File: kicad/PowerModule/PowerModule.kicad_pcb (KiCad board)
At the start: 4 copper layers, 85.6 x 54 mm, 58 parts, among them J1 DC+, J2 Power_out, J3 DC-, J4 105313-1206, Q3 EPC2304, Q4 EPC2304, Q5 EPC2304, Q6 EPC2304, U1 1EDN7550B, U2 1EDN7550B, U3 1EDN7550B, U4 1EDN7550B

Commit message: Power module: LS drivers next to the LS FETs, reference labels and owner block on silkscreen
- U2/U4 moved from the driver column to the top side between the phases, outputs facing the LS
  gate vias: driver -> gate path 4.8 mm (was 11-14 mm); HS 5.9-6.8 mm
- every reference designator on the silkscreen (0.8 mm, collision-checked placement)
- bottom silkscreen: owner name block, 2.3 mm text
- shield planes: 0.25 mm antipads and L2-L3 ties; centre-tap vias placed clear of the driver cells
- DRC with schematic parity: 0 violations, 0 unconnected, 0 parity issues

Co-Authored-By: Claude Opus 5.5 <noreply@anthropic.com>
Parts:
- moved D2 23.5 mm to (139.7, 128.3)
- moved R10 17.7 mm to (138.7, 126.1), turned to 180 degrees
- moved R6 17.3 mm to (132.1, 125.6)
- moved R5 17.1 mm to (132.1, 127.2)
- moved U2 16.0 mm to (135.4, 125.3), turned to 90 degrees
- moved C8 14.2 mm to (138.7, 124.4)
- moved D4 14.0 mm to (135.4, 139.4)
- moved R14 11.5 mm to (134.6, 121.6), turned to -90 degrees
- moved R13 10.6 mm to (136.2, 121.6), turned to -90 degrees
- moved R12 9.99 mm to (135.0, 137.3), turned to 180 degrees
- moved R3 9.20 mm to (132.1, 129.6)
- moved R4 8.83 mm to (132.1, 131.2)
- moved U4 8.25 mm to (135.4, 131.2), turned to -90 degrees
- moved C14 7.15 mm to (128.5, 132.2)
- moved R20 6.90 mm to (136.2, 134.8), turned to 90 degrees
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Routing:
- net +5V_iso: track 68.7 -> 92.6 mm
- net Net-(AT1-B1): track 5.71 -> 24.6 mm
- net GNDPWR: track 89.8 -> 76.6 mm, vias 396 -> 395
- net Net-(AT2-B1): track 8.62 -> 17.9 mm
- net /Gate_Drive/P1L: track 11.9 -> 2.77 mm
- net Net-(U2-IN-): track 8.57 -> 1.87 mm
- net /Gate_Drive/P2L: track 8.89 -> 2.77 mm
- net Net-(D4-K): track 8.33 -> 2.86 mm
- net Net-(U4-IN-): track 9.49 -> 4.12 mm
- net Net-(D2-K): track 7.92 -> 2.71 mm
- net Net-(U4-VDD): track 3.43 -> 6.07 mm
- net Net-(U2-IN+): track 1.91 -> 4.11 mm
- net Net-(AT2-B2): track 17.9 -> 16.6 mm, vias 2 -> 0
- net Net-(AT2-A2): track 5.50 -> 4.61 mm
- net +5V: track 49.0 -> 48.4 mm, vias 1 -> 2
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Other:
- board text added: "Tanishq Shendokar MS Electrical Engineering NC State University tsshendo@ncsu.edu +1 (336) 405-3942"

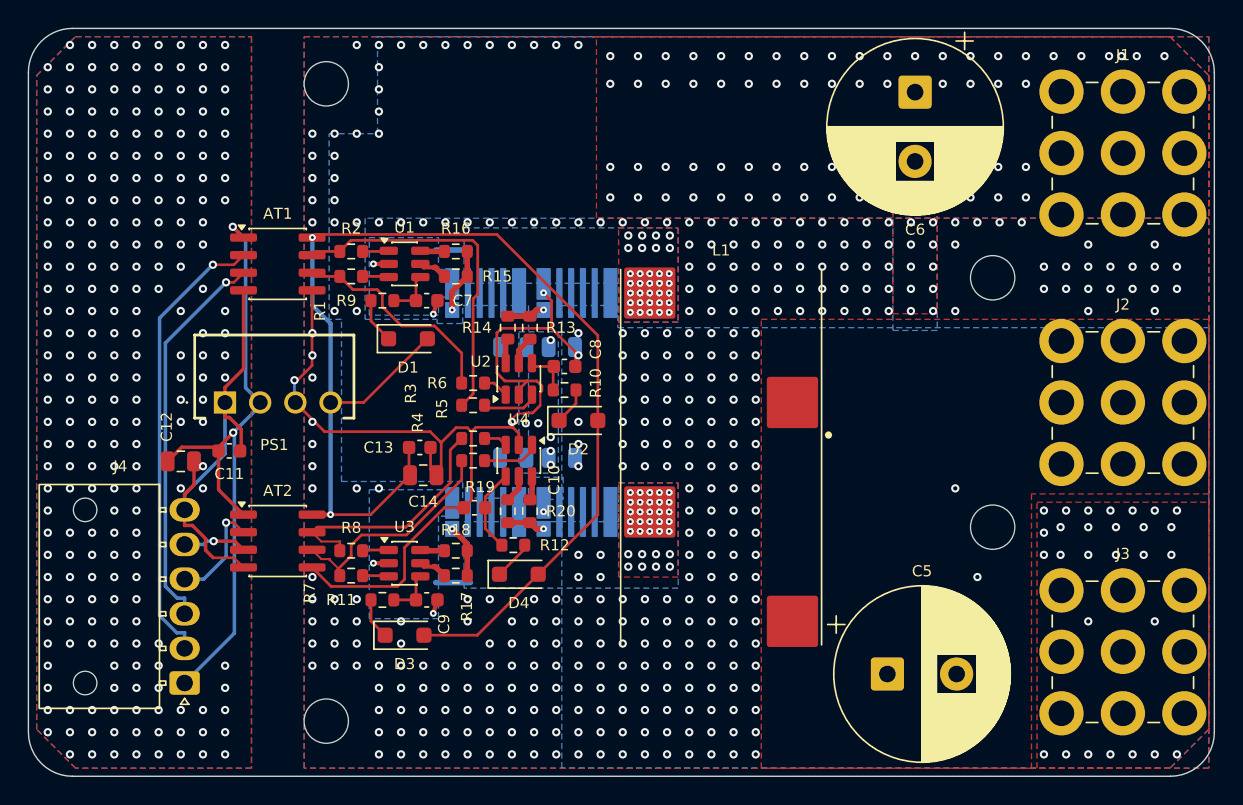
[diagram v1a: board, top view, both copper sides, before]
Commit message: Power module: bulk caps split into 4 x 62 uF, J4 centred with fixed control lanes
- C5/C6 -> C5+C15 (output), C6+C16 (input): 2 x EGXF161ELL620MJ25S per position (user: half
  values for lower ESR); VIN/VOUT labels added (pm_split_bulk.py), ERC 0 errors
- J4 centred on the left edge; AT1 pair on L4, AT2 pair on L1, +5V lane on L4: 15-19 mm per
  command line, no meanders; PS1 to the bottom left, H2 screw to (28.4, 50.6)
- PS1 barrier keep-out from pin-2 to pin-3 centre (1.5 mm per side)
- name block on the bottom silkscreen auto-sized into the clear strip (2.0 mm)
- DRC with schematic parity: 0 violations, 0 unconnected, 0 parity issues

Co-Authored-By: Claude Opus 5.5 <noreply@anthropic.com>
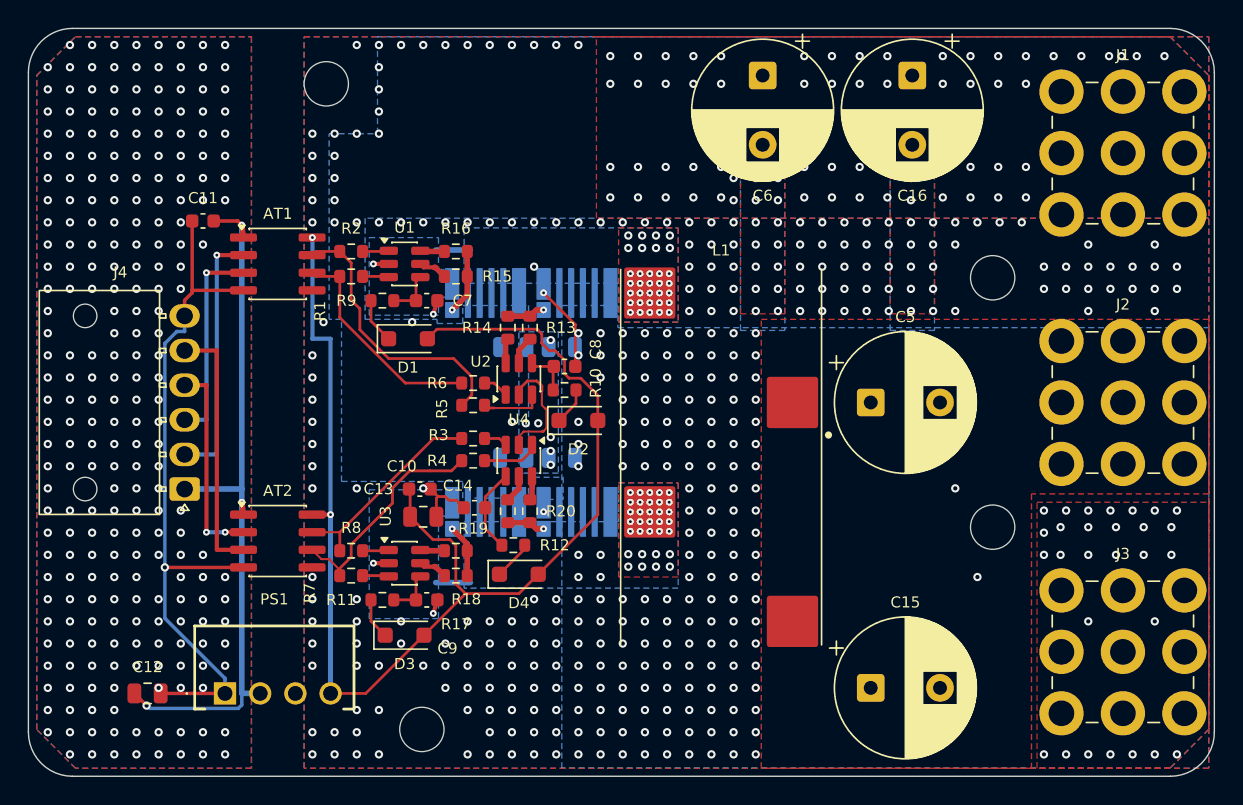
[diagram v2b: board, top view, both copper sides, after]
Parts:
- added C15: 62u/160V, Capacitor_THT:CP_Radial_D10.0mm_P5.00mm, F.Cu at (160.8, 147.6)
- added C16: 62u/160V, Capacitor_THT:CP_Radial_D10.0mm_P5.00mm, F.Cu at (163.8, 103.4)
- C5, C6: value 110u/160V -> 62u/160V; footprint Capacitor_THT:CP_Radial_D12.5mm_P5.00mm -> Capacitor_THT:CP_Radial_D10.0mm_P5.00mm
- moved PS1 21.0 mm to (114.2, 148.0)
- moved C5 19.6 mm to (160.8, 127.0)
- moved C12 16.9 mm to (108.6, 148.0)
- moved C11 16.7 mm to (112.6, 113.9), turned to 180 degrees
- moved J4 14.0 mm to (111.3, 133.2)
- moved C6 11.1 mm to (153.0, 103.4)
- moved H2 6.93 mm to (128.4, 150.6)
- moved C13 3.00 mm to (128.2, 133.2)
- moved C14 3.00 mm to (128.5, 135.2)
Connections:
- net Net-(J1-Pin_1) renamed /VIN
- net Net-(J2-Pin_1) renamed /VOUT
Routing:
- net GNDPWR: track 76.6 -> 19.9 mm, vias 395 -> 393
- net GND: track 32.7 -> 51.1 mm, vias 233 -> 243
- net +5V_iso: track 92.6 -> 107.2 mm
- net Net-(AT1-A1): track 32.9 -> 18.6 mm
- net Net-(AT2-A2): track 4.61 -> 18.6 mm, vias 1 -> 0
- net Net-(AT1-A2): track 28.2 -> 14.9 mm
- net Net-(AT2-A1): track 7.67 -> 14.9 mm, vias 1 -> 2
- net Net-(AT1-B1): track 24.6 -> 20.2 mm
- net +5V: track 48.4 -> 52.1 mm, vias 2 -> 3
- net Net-(AT2-B1): track 17.9 -> 14.9 mm
- net /VIN: vias 66 -> 57
- net /SHIELD: vias 7 -> 9

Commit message: Power module: symmetric bulk caps, PS1 centred on J4, right-angle J4 with model
- bulk caps mirror-symmetric: C6/C16 on the top edge (VBUS), C5/C15 on the bottom edge (VOUT
  strip added), x 37.5 / 64.6; PGND tongues for C6 (L1 + vias) and C16
- PS1 on J4's centreline; J4 right angle, mating face 2.2 mm off the edge; H2 back to (21.5, 50)
- J4 project footprint Molex_Nano-Fit_105313-1206_RA (off-board silk dropped) + generated
  right-angle STEP (gen_footprints.py, nanofit_fp.py)
- name block 2.35 mm in the widened clear strip
- ERC 0 errors; DRC with schematic parity: 0 violations, 0 unconnected, 0 parity issues

Co-Authored-By: Claude Opus 5.5 <noreply@anthropic.com>
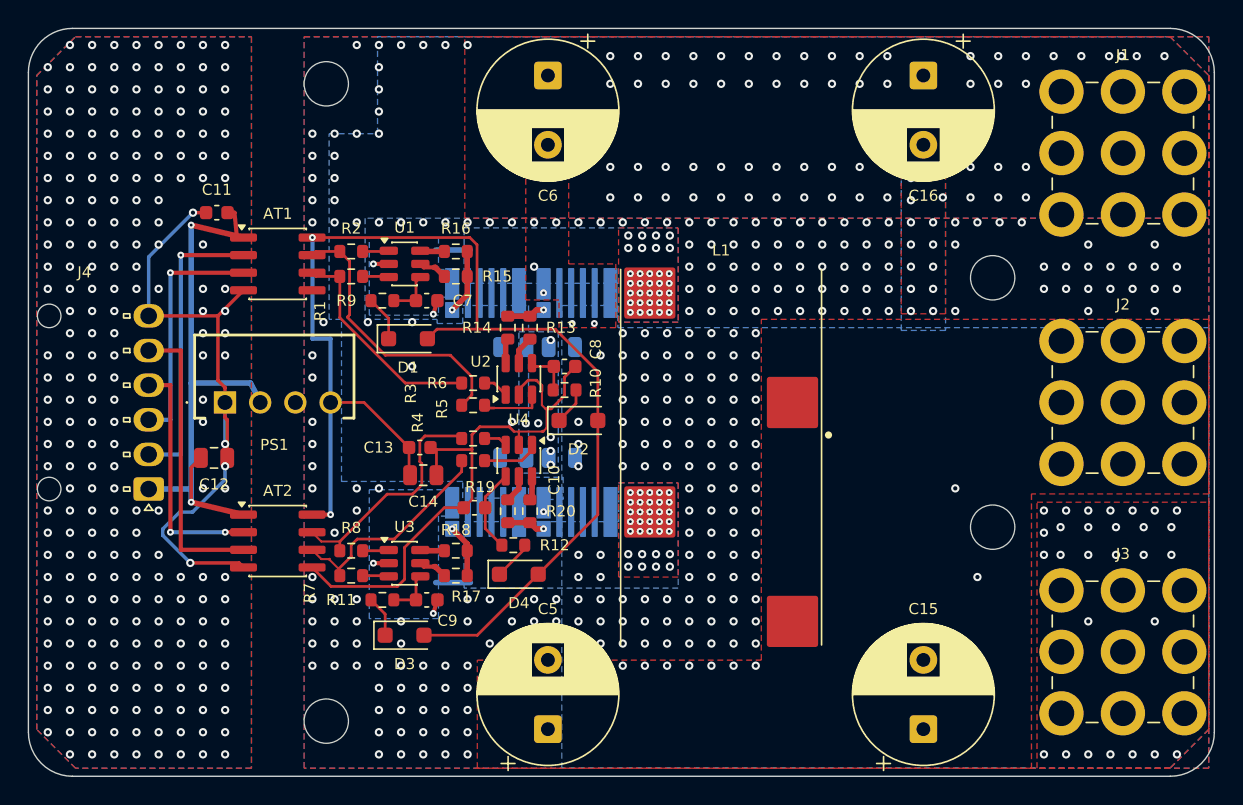
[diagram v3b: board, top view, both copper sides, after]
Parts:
- J4: footprint Connector_Molex:Molex_Nano-Fit_105313-xx06_1x06_P2.50mm_Horizontal -> ECE533_Mods:Molex_Nano-Fit_105313-1206_RA
- moved C5 33.1 mm to (137.5, 150.6), turned to 90 degrees
- moved PS1 21.0 mm to (114.2, 127.0)
- moved C12 17.7 mm to (113.4, 131.0)
- moved C6 15.5 mm to (137.5, 103.4)
- moved H2 6.93 mm to (121.5, 150.0)
- moved C15 4.83 mm to (164.6, 150.6), turned to 90 degrees
- moved C13 3.00 mm to (128.2, 130.2)
- moved C14 3.00 mm to (128.5, 132.2)
- moved J4 2.59 mm to (108.7, 133.2)
- moved C11 1.17 mm to (113.6, 113.3)
- moved C16 0.80 mm to (164.6, 103.4)
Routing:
- net GNDPWR: track 19.9 -> 42.9 mm, vias 393 -> 333
- net +5V_iso: track 107.2 -> 90.2 mm
- net +5V: track 52.1 -> 41.6 mm, vias 3 -> 2
- net GND: track 51.1 -> 46.6 mm, vias 243 -> 238
- net Net-(AT2-A2): track 18.6 -> 21.2 mm
- net Net-(AT2-A1): track 14.9 -> 17.5 mm
- net Net-(AT1-A2): track 14.9 -> 17.5 mm
- net Net-(AT1-A1): track 18.6 -> 21.2 mm
- net Net-(AT2-B1): track 14.9 -> 17.0 mm
- net /VIN: vias 57 -> 63
- net /SHIELD: vias 9 -> 11

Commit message: Power module: 1 kOhm gate pull-downs R21-R24 at the gate pads
- schematic: R21 P1H-KS1, R22 P1L-GNDPWR, R23 P2H-KS2, R24 P2L-GNDPWR (pm_pulldowns.py), as in
  the report's LTspice model; ERC 0 errors
- HS pull-downs on the bottom inside the Kelvin island next to the gate pads, LS on the top over
  the gate via next to the LS Kelvin via
- DRC with schematic parity: 0 violations, 0 unconnected, 0 parity issues; BOM and docs updated

Co-Authored-By: Claude Opus 5.5 <noreply@anthropic.com>
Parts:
- added R21: 1k, Resistor_SMD:R_0603_1608Metric, B.Cu at (128.2, 120.3)
- added R22: 1k, Resistor_SMD:R_0603_1608Metric, F.Cu at (138.2, 119.7)
- added R23: 1k, Resistor_SMD:R_0603_1608Metric, B.Cu at (128.2, 136.1)
- added R24: 1k, Resistor_SMD:R_0603_1608Metric, F.Cu at (138.2, 135.5)
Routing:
- net GNDPWR: track 42.9 -> 49.1 mm
- net GND: track 46.6 -> 41.6 mm, vias 238 -> 237
- net Net-(AT2-B2): track 16.3 -> 19.4 mm
- net /Gate_Drive/P2H: track 3.83 -> 5.39 mm
- net /Gate_Drive/P1H: track 4.67 -> 6.23 mm
- net /Gate_Drive/P1L: track 2.77 -> 3.81 mm
- net /Gate_Drive/P2L: track 2.77 -> 3.81 mm
- net /SHIELD: vias 11 -> 8

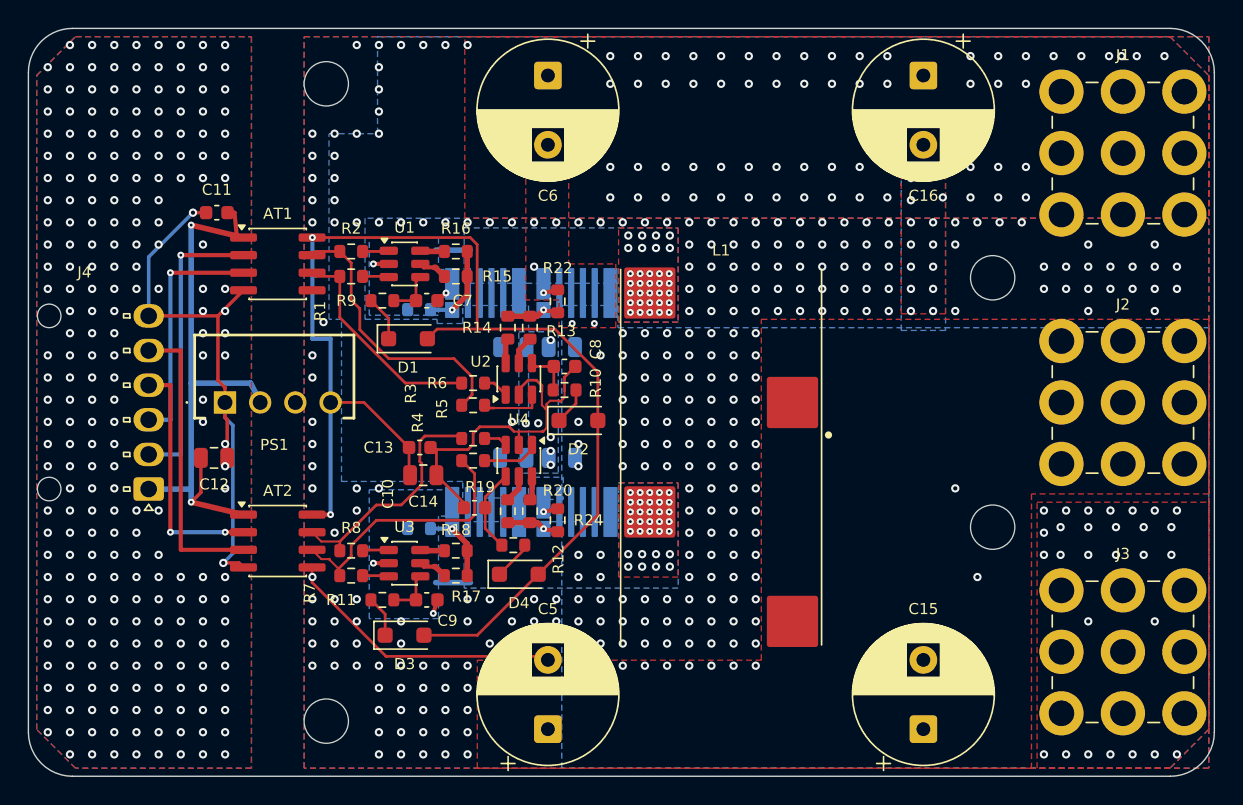
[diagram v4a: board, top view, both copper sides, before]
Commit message: Power module: centred inductor, symmetric control side, bulk caps grouped by role
- inductor body centred on the board; L4/L1 switch-node copper extended under its SW pads
- gate-drive cells as identical per-phase copies (15.8 mm pitch): both phases HS 8.3 / LS 5.9 mm;
  Kelvin islands copied; isolators, PS1, J4, C11/C12 mirrored about the centreline
- input bulk C6 + C16 on the top edge (input side, L1 PGND tongue to the LS1 comb), output bulk
  C5 + C15 on the bottom edge under the VOUT pads
- DRC with schematic parity: 0 violations, 0 unconnected, 0 parity issues

Co-Authored-By: Claude Opus 5.5 <noreply@anthropic.com>
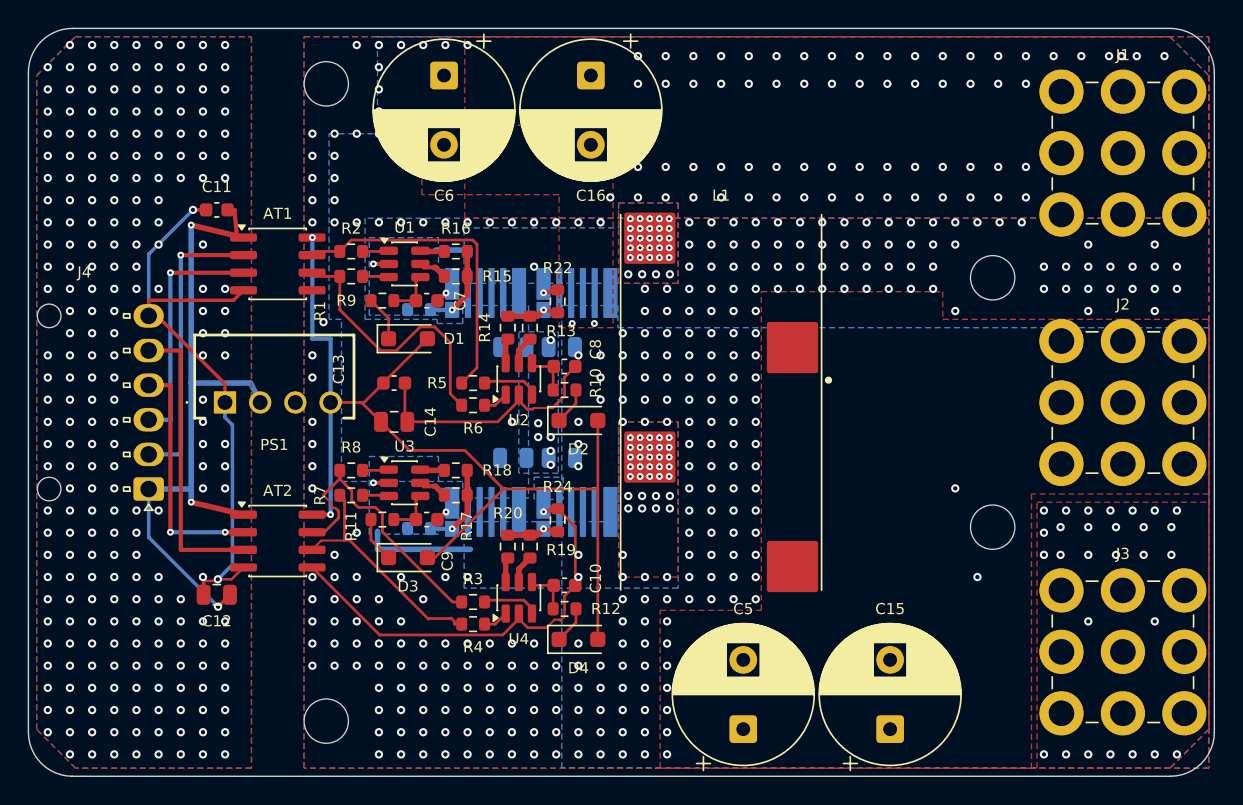
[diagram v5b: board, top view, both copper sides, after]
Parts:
- moved C16 24.0 mm to (140.6, 103.4)
- moved C5 14.1 mm to (151.6, 150.6)
- moved R3 11.8 mm to (132.1, 141.4)
- moved R4 11.8 mm to (132.1, 143.0)
- moved U4 9.90 mm to (135.4, 141.1), turned to 90 degrees
- moved C12 9.88 mm to (113.6, 140.9), turned to 180 degrees
- moved C10 8.58 mm to (138.7, 140.2), turned to 0 degrees
- moved C6 7.50 mm to (130.0, 103.4)
- moved D4 6.37 mm to (139.7, 144.1)
- moved R12 5.90 mm to (138.7, 141.9)
- moved C9 5.80 mm to (128.8, 135.4)
- moved R11 5.80 mm to (125.5, 135.4)
- moved R17 5.80 mm to (130.8, 133.7)
- moved R7 5.80 mm to (123.3, 133.7)
- moved R18 5.80 mm to (130.8, 131.9)
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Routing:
- net +5V_iso: track 90.2 -> 74.5 mm
- net +5V: track 41.6 -> 50.1 mm, vias 2 -> 3
- net /Gate_Drive/KS2: track 4.63 -> 9.94 mm
- net Net-(AT1-B2): track 15.8 -> 19.8 mm
- net GND: track 41.6 -> 45.1 mm, vias 237 -> 235
- net Net-(AT2-B1): track 17.0 -> 20.4 mm
- net Net-(AT1-B1): track 20.2 -> 23.0 mm
- net Net-(U4-VDD): track 6.07 -> 3.37 mm
- net Net-(U4-IN+): track 1.72 -> 4.10 mm
- net GNDPWR: track 49.1 -> 51.5 mm, vias 333 -> 348
- net Net-(AT2-B2): track 19.4 -> 17.1 mm
- net Net-(U4-IN-): track 4.10 -> 1.84 mm
- net /Gate_Drive/P2H: track 5.39 -> 6.23 mm
- net /VIN: vias 63 -> 67
- net /Gate_Drive/KS1: vias 35 -> 31
